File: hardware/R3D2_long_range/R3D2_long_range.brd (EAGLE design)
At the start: 70 x 65.3 mm, 64 parts, among them IC1 ATXMEGA64DA-AU, IC2 NCV8774DT33RKG, IC3 MAX3232CSE, T1 MMBT2222LT1G, T2 ZXMP6A17E6TA, T3 DMN6068SE

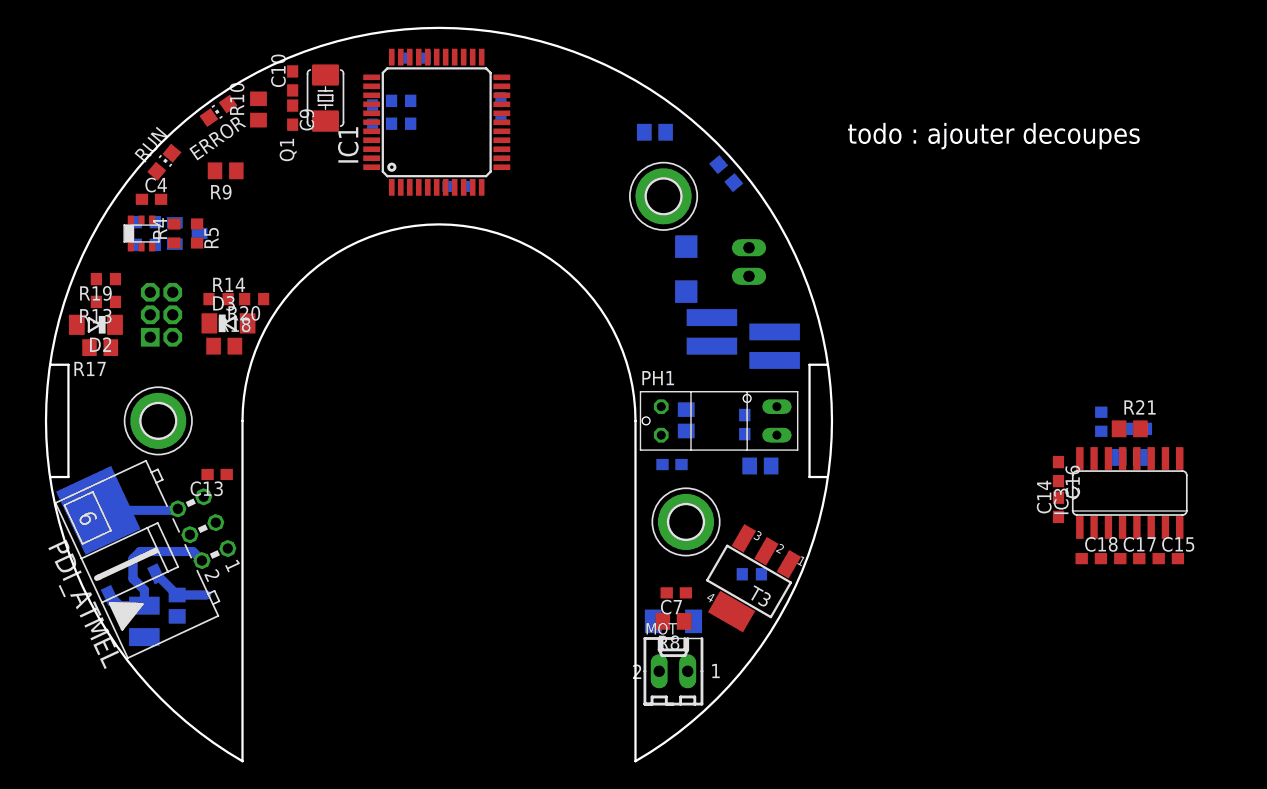
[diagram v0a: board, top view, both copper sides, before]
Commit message: routing board and remarks taken into account in sch
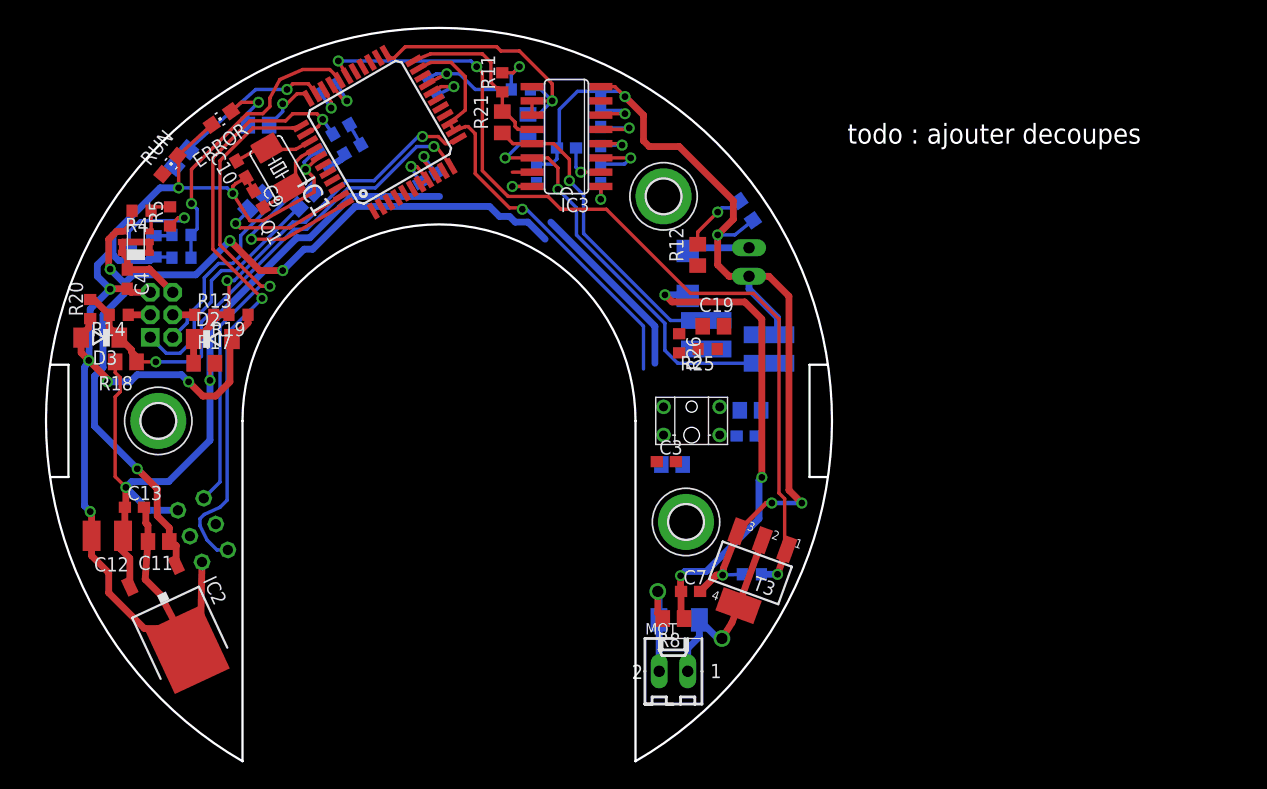
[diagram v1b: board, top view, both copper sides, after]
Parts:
- added C19: 100nF 50V, robotter_capacitor:C0805
- added R23, R24: 270-E, robotter_resistor:R0805
- added R25: 10K-F, robotter_resistor:R0603
- added R26: 150K-F, robotter_resistor:R0603
- IC1: value ATXMEGA64DA-AU -> ATXMEGA64D4-AU
- PH1: value GP1S58VJ000F -> EESX1106; device robotter_ic:GP1S58VJ000F -> robotter_ic:EESX1106
- moved C15 64.9 mm to (49.4, 63.5), flipped to the bottom, turned to 90 degrees
- moved R16 62.6 mm to (42.3, 64.5)
- moved R21 62.2 mm to (40.6, 61.6), turned to 90 degrees
- moved R11 61.3 mm to (40.6, 65.2), flipped to the top, turned to 90 degrees
- moved R22 61.2 mm to (42.9, 61.3), turned to 90 degrees
- moved C17 60.3 mm to (49.4, 60.3), flipped to the bottom, turned to 90 degrees
- moved IC3 59.4 mm to (46.4, 60.3), turned to 90 degrees
- moved C18 55.5 mm to (49.4, 57.0), flipped to the bottom, turned to 90 degrees
- moved C14 54.3 mm to (46.4, 59.3), flipped to the bottom, turned to 0 degrees
- moved C16 53.5 mm to (43.7, 57.0), flipped to the bottom, turned to 90 degrees
- moved R20 14.6 mm to (3.94, 45.0), turned to 90 degrees
- moved R19 12.2 mm to (17.1, 44.5)
- moved R12 11.6 mm to (58.0, 49.8), flipped to the top, turned to 90 degrees
- moved D3 11.5 mm to (4.83, 42.4), turned to 180 degrees
- moved D2 10.5 mm to (14.9, 42.3), turned to 0 degrees
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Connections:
- removed net N$12: IC1.33, R12.1
- new net LED_COM_3V3: IC1.10, R12.1
- new net N$17: IR-SENSOR.2, R23.1
- new net N$18: IR-SENSOR.1, R24.1
- new net VBAT_0-2V: C19.1, IC1.6, R25.2, R26.1
- net +24V: now also R26.2
- net GND: now also C19.2, IC1.7, PH1.E, PH1.K, R25.1; no longer PH1.LED_C, PH1.TRANSISTOR_E
- net LONG_RANGE_LED_3V3: now also IC1.43, R23.2; no longer IC1.4, IR-SENSOR.2
- net LONG_RANGE_SENSOR_OUTPUT_3V3: now also IC1.12; no longer IC1.11
- net MIRROR_INDEX_3V3: now also IC1.13, IC1.21, PH1.C; no longer IC1.15, PH1.TRANSISTOR_C
- net MOTOR_PWM_3V3: now also IC1.28; no longer IC1.20
- net N$10: now also IC1.33; no longer IC1.32
- net N$15: now also PH1.A; no longer PH1.LED_A
- net N$9: now also IC1.32; no longer IC1.29
- net ON/OFF_SENSOR_3V3: now also IC1.29
- net SHORT_RANGE_LED_3V3: now also IC1.44, R24.2; no longer IC1.5, IR-SENSOR.1
- net SHORT_RANGE_SENSOR_OUTPUT_3V3: now also IC1.11; no longer IC1.12
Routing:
- net GND: track 7.14 -> 242.6 mm, vias 0 -> 16
- net +24V: track 5.30 -> 123.7 mm, vias 0 -> 7
- net +3V3: track 14.8 -> 117.9 mm, vias 0 -> 7
- net MOTOR_PWM_3V3: track 0.00 -> 80.0 mm, vias 0 -> 3
- net /RESET_3V3: track 0.00 -> 56.1 mm, vias 0 -> 2
- net SHORT_RANGE_SENSOR_OUTPUT_3V3: track 0.00 -> 46.1 mm, vias 0 -> 2
- net PDI_DATA_3V3: track 0.00 -> 43.7 mm, vias 0 -> 1
- net MIRROR_INDEX_3V3: track 0.00 -> 40.7 mm, vias 0 -> 1
- net TX_232: track 0.00 -> 37.9 mm, vias 0 -> 2
- net LONG_RANGE_SENSOR_OUTPUT_3V3: track 0.00 -> 36.0 mm, vias 0 -> 2
- net RX_232: track 0.00 -> 28.2 mm, vias 0 -> 1
- net TX_3V3: track 0.00 -> 26.4 mm, vias 0 -> 1
- net ON/OFF_SENSOR_3V3: track 0.00 -> 26.2 mm, vias 0 -> 1
- net N$18: track 0.00 -> 21.4 mm
- net MOTOR_M: track 0.00 -> 17.2 mm, vias 0 -> 1
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
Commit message: board V1 routed
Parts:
- moved R6 7.25 mm to (55.4, 38.4)
- moved C3 7.11 mm to (55.4, 38.5), turned to 180 degrees
- moved R1 1.59 mm to (61.3, 35.2), turned to 270 degrees
- moved PH1 1.50 mm to (56.0, 35.0)
- moved C1 1.26 mm to (63.2, 34.5), turned to 270 degrees
- moved R26 1.02 mm to (56.4, 42.9), turned to 90 degrees
- moved C16 0.13 mm to (43.7, 57.1)
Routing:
- net GND: track 242.6 -> 314.0 mm, vias 16 -> 17
- net +3V3: track 117.9 -> 174.4 mm, vias 7 -> 11
- net VBAT_0-2V: track 0.00 -> 34.3 mm
- net LED_COM_3V3: track 0.00 -> 27.3 mm, vias 0 -> 2
- net +24V: track 123.7 -> 138.3 mm, vias 7 -> 8
- net MIRROR_INDEX_3V3: track 40.7 -> 46.3 mm
- net N$2: track 0.00 -> 4.97 mm, vias 0 -> 1
- net N$16: track 1.86 -> 6.68 mm, vias 0 -> 1
- net N$15: track 0.00 -> 2.89 mm
- net N$1: track 2.58 -> 3.09 mm
- added copper zone on layer 1, net GND
- added copper zone on layer 16, net GND
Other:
- board size 70 x 65.3 mm -> 69.3 x 65.3 mm
- board text added: "R3D2_long_range"
- board text added: "Robotter"
- board text added: "V1"
- board text removed: "todo : ajouter decoupes"

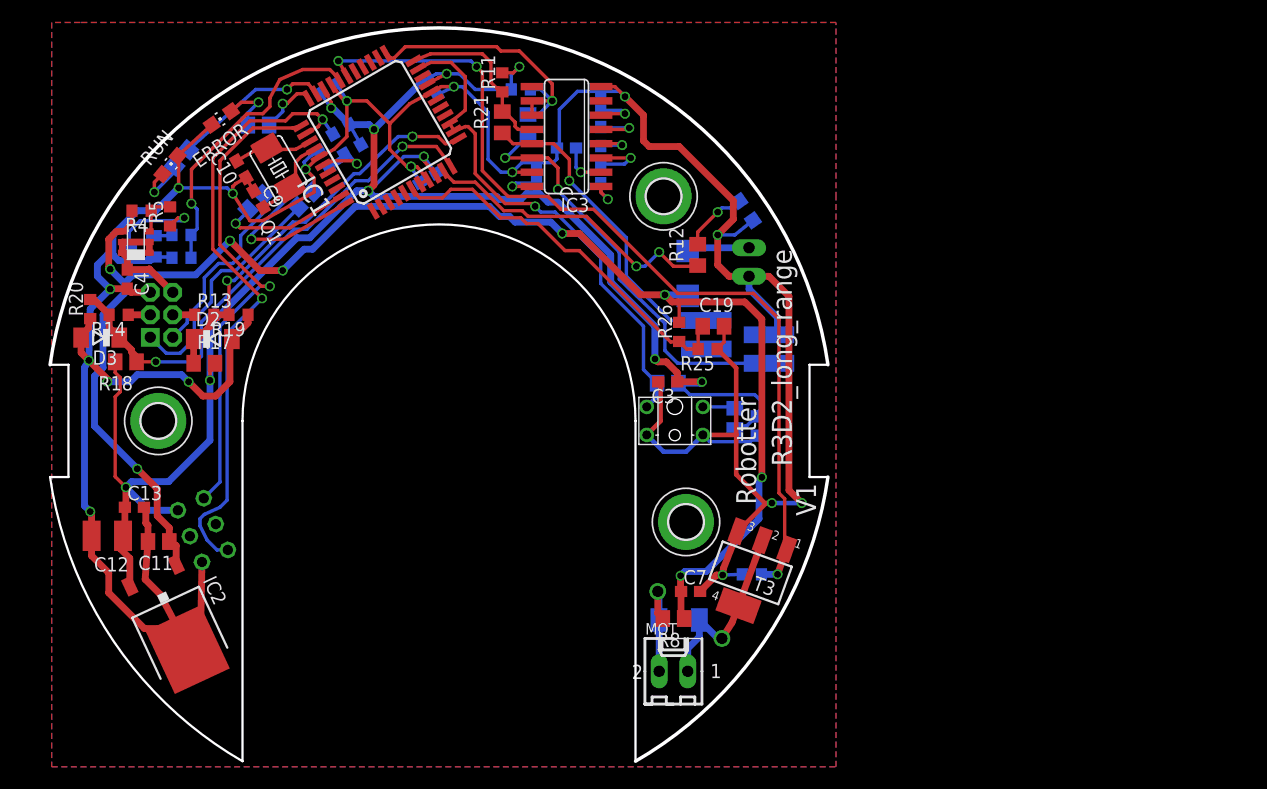
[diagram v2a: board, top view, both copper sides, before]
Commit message: some via added to the ground plane
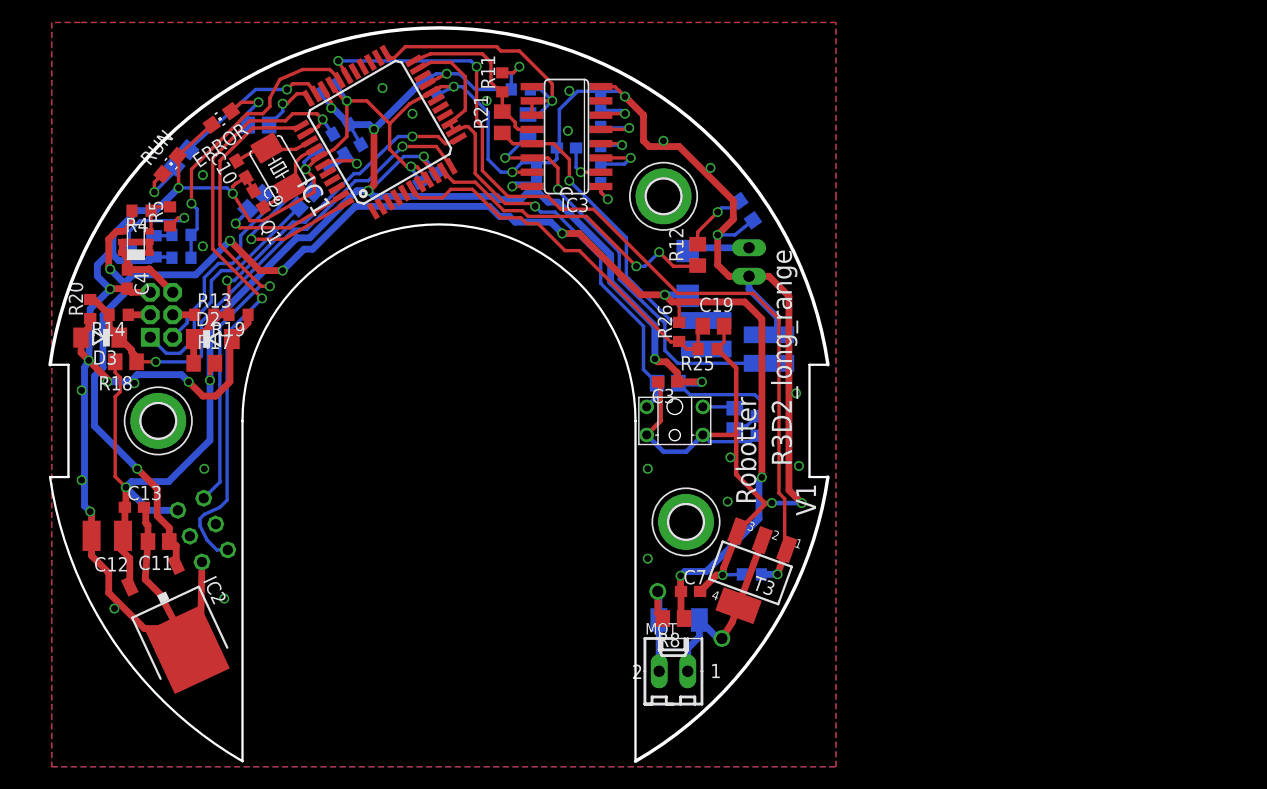
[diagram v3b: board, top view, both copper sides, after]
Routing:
- net GND: vias 17 -> 38
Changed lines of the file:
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@@
 <vertex x="0.508" y="70.485"/>
 </polygon>
+<via x="13.97" y="56.896" extent="1-16" drill="0.6" shape="octagon"/>
+<via x="13.97" y="50.546" extent="1-16" drill="0.6" shape="octagon"/>
+<via x="39.243" y="63.5" extent="1-16" drill="0.6" shape="octagon"/>
+<via x="54.991" y="59.944" extent="1-16" drill="0.6" shape="octagon"/>
+<via x="59.182" y="57.531" extent="1-16" drill="0.6" shape="octagon"/>
+<via x="67.056" y="30.988" extent="1-16" drill="0.6" shape="octagon"/>
+<via x="66.802" y="37.465" extent="1-16" drill="0.6" shape="octagon"/>
+<via x="60.96" y="31.75" extent="1-16" drill="0.6" shape="octagon"/>
+<via x="53.594" y="30.734" extent="1-16" drill="0.6" shape="octagon"/>
+<via x="53.594" y="22.733" extent="1-16" drill="0.6" shape="octagon"/>
+<via x="60.706" y="27.813" extent="1-16" drill="0.6" shape="octagon"/>
+<via x="7.874" y="38.354" extent="1-16" drill="0.6" shape="octagon"/>
+<via x="3.175" y="37.719" extent="1-16" drill="0.6" shape="octagon"/>
+<via x="3.175" y="29.718" extent="1-16" drill="0.6" shape="octagon"/>
+<via x="14.097" y="30.734" extent="1-16" drill="0.6" shape="octagon"/>
+<via x="6.096" y="18.288" extent="1-16" drill="0.6" shape="octagon"/>
+<via x="15.875" y="19.177" extent="1-16" drill="0.6" shape="octagon"/>
+<via x="29.972" y="64.643" extent="1-16" drill="0.6" shape="octagon"/>
+<via x="32.639" y="62.357" extent="1-16" drill="0.6" shape="octagon"/>
+<via x="46.609" y="64.389" extent="1-16" drill="0.6" shape="octagon"/>
+<via x="46.482" y="60.833" extent="1-16" drill="0.6" shape="octagon"/>
 </signal>
 <signal name="+3V3">
@@
 <wire x1="44.704" y1="54.991" x2="41.148" y2="54.991" width="0.3048" layer="1"/>
 <wire x1="41.148" y1="54.991" x2="38.862" y2="57.277" width="0.3048" layer="1"/>
-<wire x1="38.862" y1="57.277" x2="38.862" y2="66.04" width="0.3048" layer="1"/>
-<wire x1="38.862" y1="66.04" x2="38.354" y2="66.548" width="0.3048" layer="1"/>
+<wire x1="38.862" y1="57.277" x2="38.862" y2="61.214" width="0.3048" layer="1"/>
+<wire x1="38.862" y1="61.214" x2="38.354" y2="61.722" width="0.3048" layer="1"/>
+<wire x1="38.354" y1="61.722" x2="38.354" y2="66.548" width="0.3048" layer="1"/>
 <wire x1="65.786" y1="28.067" x2="65.278" y2="28.575" width="0.3048" layer="1"/>
 <wire x1="65.278" y1="28.575" x2="65.278" y2="44.069" width="0.3048" layer="1"/>

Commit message: com led moved to be viewable with others debug leds
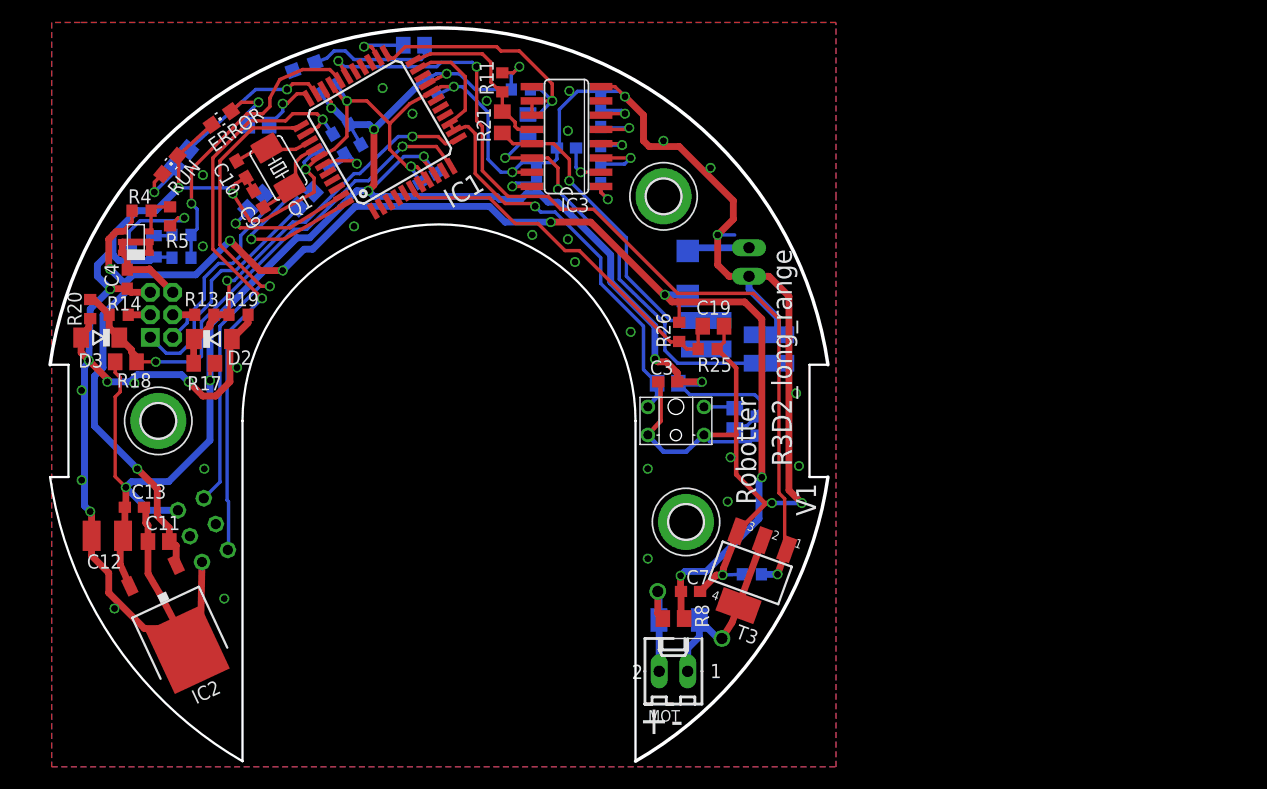
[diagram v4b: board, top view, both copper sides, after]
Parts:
- moved COM 41.4 mm to (23.0, 66.5), turned to 250 degrees
- moved R12 31.4 mm to (32.8, 68.5), flipped to the bottom, turned to 180 degrees
- moved PH1 0.10 mm to (56.1, 35.0)
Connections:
- net LED_COM_3V3: now also IC1.24; no longer IC1.10
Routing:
- net LED_COM_3V3: track 27.3 -> 5.37 mm, vias 2 -> 1
- net N$7: track 5.90 -> 11.5 mm, vias 1 -> 0
- net /RESET_3V3: track 56.1 -> 53.4 mm
- net GND: track 314.0 -> 311.4 mm, vias 38 -> 44
- net VBAT_0-2V: track 34.3 -> 33.7 mm
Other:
- board text added: "+"
- board text added: "-"

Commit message: R3D2_long_range : some comments added
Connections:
- net N$125 renamed SENSOR_SUPPLY
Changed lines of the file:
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@@
 <?xml version="1.0" encoding="utf-8"?>
 <!DOCTYPE eagle SYSTEM "eagle.dtd">
-<eagle version="6.5.0">
+<eagle version="7.4.0">
 <drawing>
 <settings>
@@
 <pass name="Default">
 <param name="RoutingGrid" value="50mil"/>
+<param name="AutoGrid" value="1"/>
+<param name="Efforts" value="0"/>
+<param name="TopRouterVariant" value="1"/>
 <param name="tpViaShape" value="round"/>
 <param name="PrefDir.1" value="|"/>
@@
 <wire x1="59.839" y1="15.621" x2="58.188" y2="17.272" width="0.6096" layer="16"/>
 </signal>
-<signal name="N$125">
+<signal name="SENSOR_SUPPLY">
 <contactref element="C4" pad="1"/>
 <contactref element="IR-SENSOR" pad="6"/>
